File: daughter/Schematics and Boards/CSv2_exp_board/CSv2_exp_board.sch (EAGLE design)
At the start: 133 parts, among them J1 HIROSE-DF40_44-PIN_CONNECTORS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, J2 J-SERIAL-PORT, J3 CORTEX_DEBUG_SMD, J301 HIROSE-DF40_44-PIN_CONNECTORS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, J4 SJ-43514-SMT, J7 J-USB-HIROSE-MICRO-USB, SW1 SPST_TACT-KMR2, SW2 SPST_TACT-KMR2, U1 LOADSWITCH-MIC94164, U10 LOADSWITCH-MIC94164, U11 BMI160, U12 TLV320DAC26IRHB, U13 ADG839YKSZ-500RL7KS_6_ADI-L, U14 LOADSWITCH-MIC94164, U2 ADA4841-1YRJZ-R7, U205 MPL3115A2, U3 Value, U4 RFM69HCW, U5 Value, U6 Value, U7 LOADSWITCH-MIC94164, U8 LOADSWITCH-MIC94164, U9 LOADSWITCH-MIC94164, X1 32.768kHz, X2 32.768, X3 uFL, X4 uFL, X5 uFL, X6 uFL

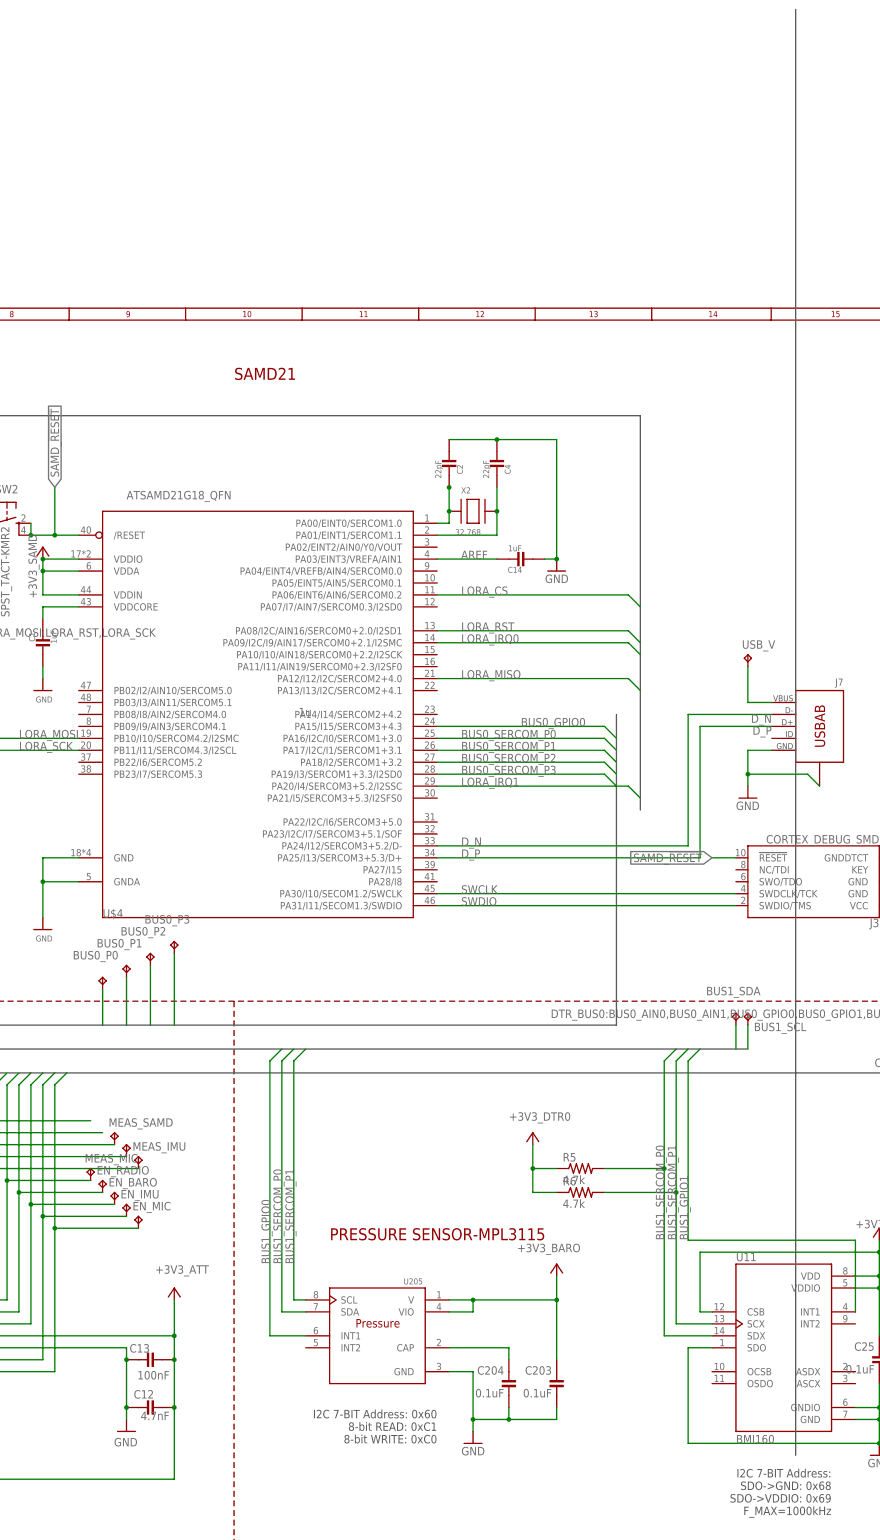
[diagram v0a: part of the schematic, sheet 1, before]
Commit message: DTR-placement + manual routing
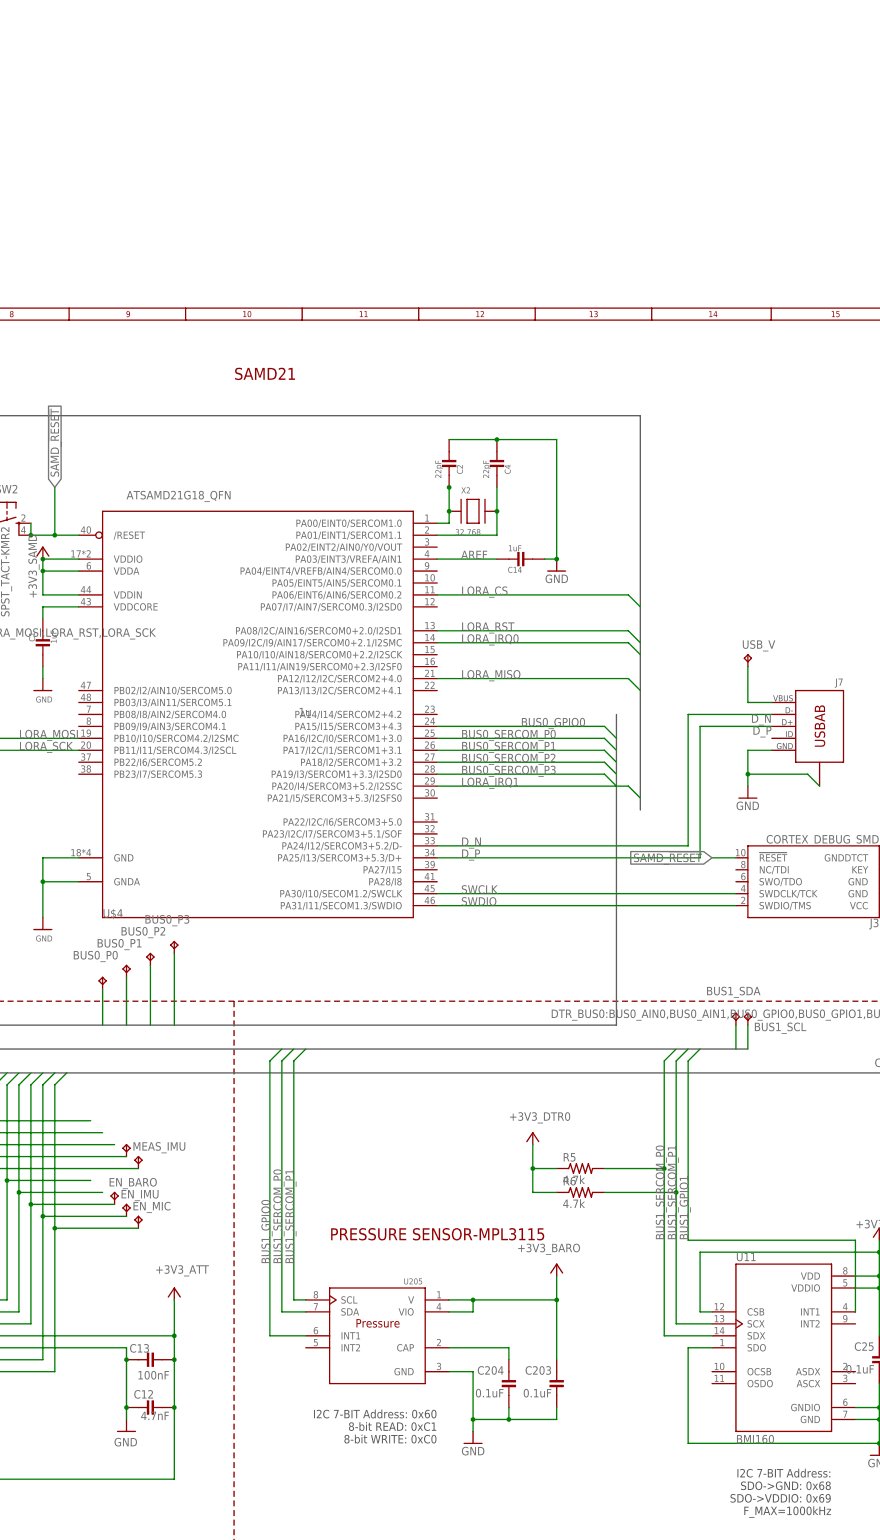
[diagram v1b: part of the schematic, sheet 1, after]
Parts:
- removed EN_RADIO, MEAS_MIC, MEAS_SAMD: TPTP10SQ, TestPoints:TPTP10SQ
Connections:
- net EN_RADIO: no longer EN_RADIO.TP
- net GND: now also U12.EPAD
- net MEAS_MIC: no longer MEAS_MIC.TP
- net MEAS_SAMD: no longer MEAS_SAMD.TP
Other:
- moved on the sheet: U12
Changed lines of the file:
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@@
 <part name="SW1" library="adafruit" library_urn="urn:adsk.eagle:library:420" deviceset="SPST_TACT" device="-KMR2" package3d_urn="urn:adsk.eagle:package:6240885/1"/>
 <part name="SW2" library="adafruit" library_urn="urn:adsk.eagle:library:420" deviceset="SPST_TACT" device="-KMR2" package3d_urn="urn:adsk.eagle:package:6240885/1"/>
-<part name="MEAS_SAMD" library="TestPoints" deviceset="TP" device="TP10SQ" package3d_urn="urn:adsk.eagle:package:27962/1" value="TPTP10SQ"/>
-<part name="MEAS_MIC" library="TestPoints" deviceset="TP" device="TP10SQ" package3d_urn="urn:adsk.eagle:package:27962/1" value="TPTP10SQ"/>
-<part name="EN_RADIO" library="TestPoints" deviceset="TP" device="TP10SQ" package3d_urn="urn:adsk.eagle:package:27962/1" value="TPTP10SQ"/>
 <part name="X3" library="Connectors" deviceset="J-U.FL" device="" value="uFL"/>
 <part name="X5" library="Connectors" deviceset="J-U.FL" device="" value="uFL"/>
@@
 <attribute name="VALUE" x="184.15" y="227.965" size="1.778" layer="96" rot="R270"/>
 </instance>
-<instance part="MEAS_SAMD" gate="G$1" x="208.28" y="99.06" smashed="yes">
-<attribute name="NAME" x="207.01" y="100.33" size="1.778" layer="95"/>
-<attribute name="TP_SIGNAL_NAME" x="209.55" y="97.79" size="1.778" layer="97"/>
-</instance>
-<instance part="MEAS_MIC" gate="G$1" x="203.2" y="91.44" smashed="yes">
-<attribute name="NAME" x="201.93" y="92.71" size="1.778" layer="95"/>
-<attribute name="TP_SIGNAL_NAME" x="204.47" y="90.17" size="1.778" layer="97"/>
-</instance>
-<instance part="EN_RADIO" gate="G$1" x="205.74" y="88.9" smashed="yes">
-<attribute name="NAME" x="204.47" y="90.17" size="1.778" layer="95"/>
-<attribute name="TP_SIGNAL_NAME" x="207.01" y="87.63" size="1.778" layer="97"/>
-</instance>
 <instance part="C26" gate="G$1" x="86.36" y="231.14" smashed="yes" rot="R90">
 <attribute name="NAME" x="84.455" y="232.156" size="1.778" layer="95" rot="R90"/>
@@
 <label x="300.99" y="123.444" size="1.778" layer="95"/>
 <wire x1="314.96" y1="121.92" x2="7.62" y2="121.92" width="0.762" layer="92"/>
-</segment>
-<segment>
-<wire x1="353.06" y1="337.82" x2="353.06" y2="30.48" width="0.762" layer="92"/>
 </segment>
 </bus>
@@
 <wire x1="203.2" y1="88.9" x2="185.42" y2="88.9" width="0.1524" layer="91"/>
 <junction x="185.42" y="88.9"/>
-<pinref part="MEAS_MIC" gate="G$1" pin="TP"/>
 </segment>
 </net>
@@
 <wire x1="208.28" y1="96.52" x2="177.8" y2="96.52" width="0.1524" layer="91"/>
 <junction x="177.8" y="96.52"/>
-<pinref part="MEAS_SAMD" gate="G$1" pin="TP"/>
 </segment>
 </net>
@@
 <wire x1="205.74" y1="86.36" x2="187.96" y2="86.36" width="0.1524" layer="91"/>
 <junction x="187.96" y="86.36"/>
-<pinref part="EN_RADIO" gate="G$1" pin="TP"/>
 </segment>
 </net>
@@
 <junction x="142.24" y="48.26"/>
 <pinref part="GND29" gate="1" pin="GND"/>
-<wire x1="142.24" y1="48.26" x2="142.24" y2="22.86" width="0.1524" layer="91"/>
-</segment>
-<segment>
+<wire x1="142.24" y1="48.26" x2="142.24" y2="25.4" width="0.1524" layer="91"/>
+<pinref part="U12" gate="A" pin="EPAD"/>
+<wire x1="142.24" y1="25.4" x2="142.24" y2="22.86" width="0.1524" layer="91"/>
+<wire x1="132.08" y1="60.96" x2="139.7" y2="60.96" width="0.1524" layer="91"/>
+<wire x1="139.7" y1="60.96" x2="139.7" y2="25.4" width="0.1524" layer="91"/>
+<wire x1="139.7" y1="25.4" x2="142.24" y2="25.4" width="0.1524" layer="91"/>
+<junction x="142.24" y="25.4"/>
+</segment>
+<segment>

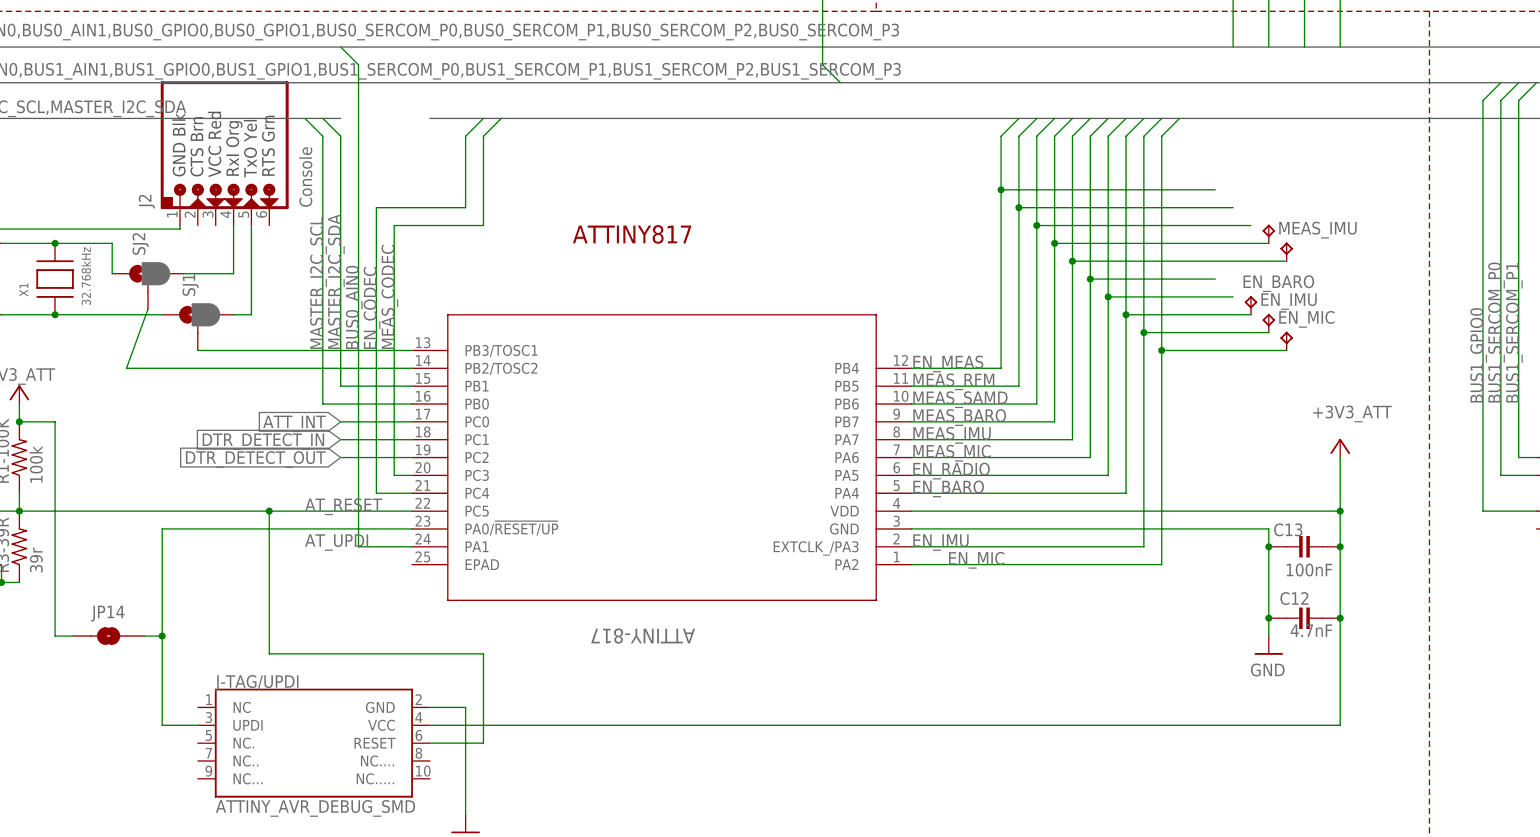
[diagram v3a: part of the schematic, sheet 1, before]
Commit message: DTR-added ldo and 80% manual routing
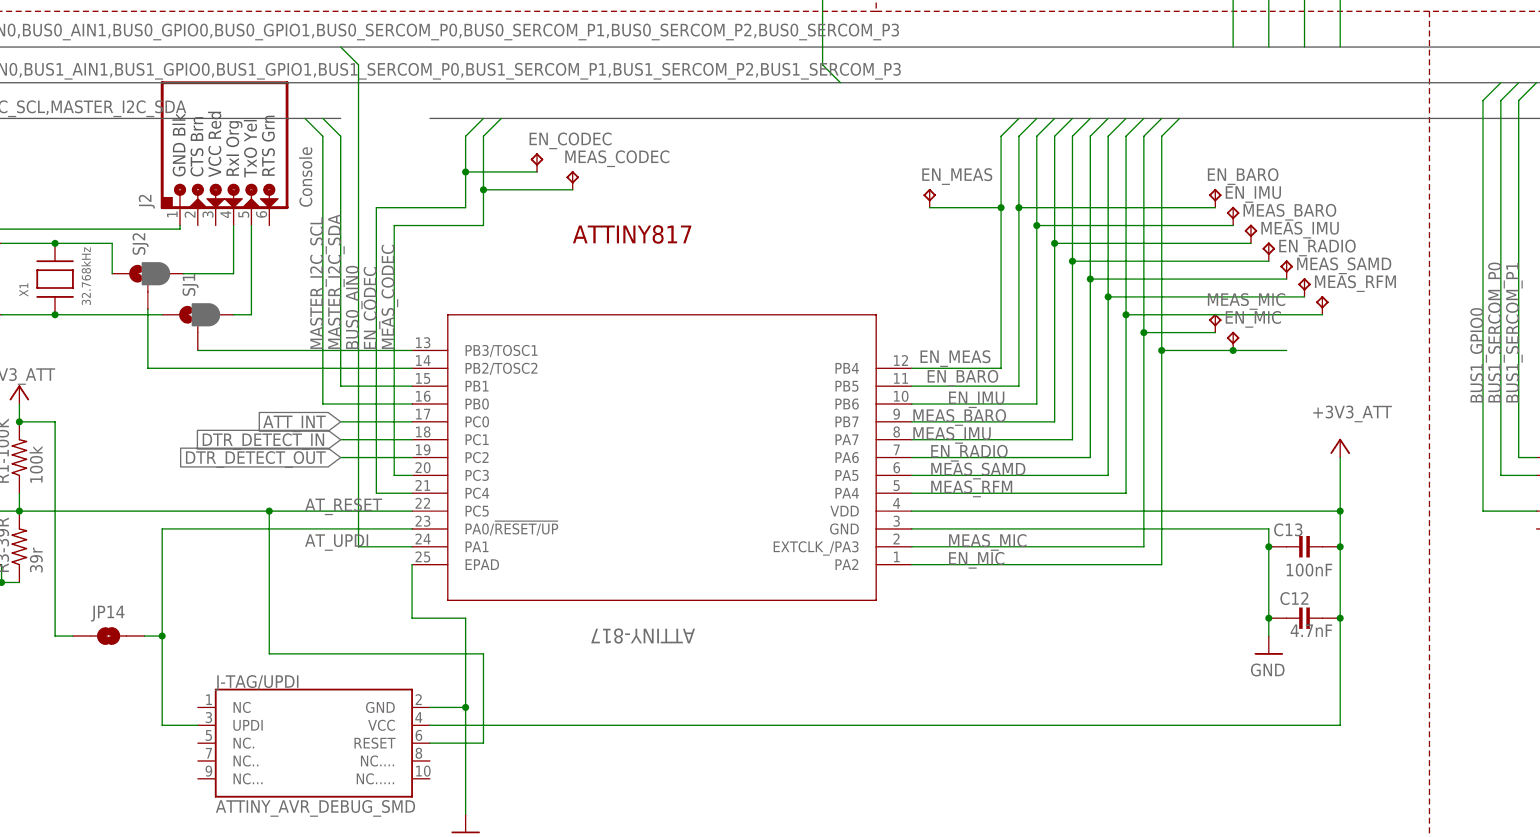
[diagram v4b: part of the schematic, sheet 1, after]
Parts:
- removed R10, R9: 100k, Resistors:R-0402
- added C41, C42: 2.2u, Capacitors:C-0402
- added EN_CODEC, EN_MEAS, EN_RADIO, MEAS_CODEC, MEAS_MIC, MEAS_RFM, MEAS_SAMD: TPTP10SQ, TestPoints:TPTP10SQ
- added U15: LP2980AIM5-2.5/NOPBMF05A_TEX-L, CommonSense-DTR-v1:LP2980AIM5-2.5/NOPBMF05A_TEX-L
- added U16: NCP553SQ18T1GSC-82AB_ONS-L, CommonSense-DTR-v1:NCP553SQ18T1GSC-82AB_ONS-L
- C35, C37, C39: device Capacitors:C-0402 -> Capacitors:C-0603
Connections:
- net N$14 renamed MICBIAS
- net N$16 renamed HPR
- net N$28 renamed MICIN
- removed net N$21: C38.1, C39.1, R10.1, R9.1, U12.DVDD
- new net +1V8_CODEC: C38.1, C39.1, U12.DVDD, U16.VOUT
- new net +3V_CODEC_A: C36.1, C37.1, U12.AVDD, U12.DRVDD, U15.VOUT
- new net HPL: C31.2, J4.TIP
- net +3V3_CODEC: now also C41.1, C42.1, U15.ON, U15.VIN, U16.VIN; no longer C36.1, C37.1, R9.2, U12.AVDD, U12.DRVDD
- net AGND: no longer C31.2, J4.TIP
- net EN_BARO: now also ATTINY-817.PB5; no longer ATTINY-817.PA4
- net EN_CODEC: now also EN_CODEC.TP
- net EN_IMU: now also ATTINY-817.PB6; no longer ATTINY-817.EXTCLK_/PA3
- net EN_MEAS: now also EN_MEAS.TP
- net EN_RADIO: now also ATTINY-817.PA6, EN_RADIO.TP; no longer ATTINY-817.PA5
- net GND: now also ATTINY-817.EPAD, C41.2, C42.2, U15.GND, U16.GND; no longer R10.2
- net MEAS_CODEC: now also MEAS_CODEC.TP
- net MEAS_MIC: now also ATTINY-817.EXTCLK_/PA3, MEAS_MIC.TP; no longer ATTINY-817.PA6
- net MEAS_RFM: now also ATTINY-817.PA4, MEAS_RFM.TP; no longer ATTINY-817.PB5
- net MEAS_SAMD: now also ATTINY-817.PA5, MEAS_SAMD.TP; no longer ATTINY-817.PB6
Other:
- moved on the sheet: EN_BARO, EN_IMU, EN_MIC, MEAS_IMU
